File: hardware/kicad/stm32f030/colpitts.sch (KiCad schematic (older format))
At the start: 42 parts, among them P2 LOOP, P3 LOOP, Q1 BSS138, Q2 BC817-40, Q3 BSS138, Q4 BC817-40, T1 78601/9C, T2 78601/9C

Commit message: hardware/kicad/stm32f030: progress
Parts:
- P2: value LOOP -> LOOP1
- P3: value LOOP -> LOOP2
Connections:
- net labels removed: Earth
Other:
- moved on the sheet: GDT2, GDT4, R14, R7

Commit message: hardware/kicad/stm32f030: progress
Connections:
- net at JP1.2, JP1.4, JP1.6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: now also T1.3 (AB); no longer T1.1 (AA)
- net at C5.1, Q1.3 (D), R1.2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: now also T1.1 (AA); no longer T1.3 (AB)
- net at GDT2.1, P2.3 (P3), T1.4 (SA): now also R7.1; no longer GDT1.2
- net at GDT1.1, P2.1 (P1), T1.6 (SB): now also GDT2.2; no longer R7.1
- net at P2.2 (P2), R7.2: now also GDT1.2; no longer GDT2.2
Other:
- moved on the sheet: GDT1, GDT2
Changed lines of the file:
@@
 P 3650 5850
 F 0 "R13" V 3550 5700 50  0000 L CNN
-F 1 "1k" V 3550 5850 50  0000 L CNN
+F 1 "1k" V 3550 5900 50  0000 L CNN
 F 2 "Resistors_SMD:R_0603_HandSoldering" H 3650 5850 50  0001 C CNN
 F 3 "" H 3650 5850 50  0000 C CNN
@@
 F 3 "" H 2600 2550 50  0000 C CNN
 	1    2600 2550
-	-1   0    0    1
+	-1   0    0    -1
 $EndComp
 $Comp
@@
 L GDT GDT1
 U 1 1 5884A6E0
+P 2100 2150
+F 0 "GDT1" H 2110 2040 60  0000 C CNN
+F 1 "GDT" H 2100 2250 60  0000 C CNN
+F 2 "gdt:CG5350L" H 2225 2325 60  0001 C CNN
+F 3 "" H 2225 2325 60  0000 C CNN
+	1    2100 2150
+	0    1    -1   0
+$EndComp
+$Comp
+L GDT GDT2
+U 1 1 5884A6E7
 P 2100 2550
-F 0 "GDT1" H 2110 2440 60  0000 C CNN
+F 0 "GDT2" H 2110 2440 60  0000 C CNN
 F 1 "GDT" H 2100 2650 60  0000 C CNN
 F 2 "gdt:CG5350L" H 2225 2725 60  0001 C CNN
 F 3 "" H 2225 2725 60  0000 C CNN
 	1    2100 2550
-	0    1    -1   0
-$EndComp
-$Comp
-L GDT GDT2
-U 1 1 5884A6E7
-P 2100 2150
-F 0 "GDT2" H 2110 2040 60  0000 C CNN
-F 1 "GDT" H 2100 2250 60  0000 C CNN
-F 2 "gdt:CG5350L" H 2225 2325 60  0001 C CNN
-F 3 "" H 2225 2325 60  0000 C CNN
-	1    2100 2150
 	0    1    -1   0
 $EndComp
@@
 F 3 "" H 1350 2550 50  0000 C CNN
 	1    1350 2550
-	-1   0    0    1
-$EndComp
-$Comp
+	-1   0    0    -1
+$EndComp
+$Comp

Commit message: hardware/kicad/stm32f030: adding eeprom step2
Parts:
- GDT1, GDT2, GDT3, GDT4: footprint gdt:CG5350L -> cardetector:GDT
- T1, T2: footprint murata_pwr:78601_9C -> cardetector:78601_9C
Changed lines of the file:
@@
 F 0 "T2" H 2600 5900 50  0000 C CNN
 F 1 "78601/9C" H 2600 5350 50  0000 C CNN
-F 2 "murata_pwr:78601_9C" H 2600 5650 50  0001 C CNN
+F 2 "cardetector:78601_9C" H 2600 5650 50  0001 C CNN
 F 3 "" H 2600 5650 50  0000 C CNN
 	1    2600 5650
@@
 F 0 "GDT3" H 2110 5540 60  0000 C CNN
 F 1 "GDT" H 2100 5750 60  0000 C CNN
-F 2 "gdt:CG5350L" H 2225 5825 60  0001 C CNN
+F 2 "cardetector:GDT" H 2225 5825 60  0001 C CNN
 F 3 "" H 2225 5825 60  0000 C CNN
 	1    2100 5650
@@
 F 0 "GDT4" H 2110 5140 60  0000 C CNN
 F 1 "GDT" H 2100 5350 60  0000 C CNN
-F 2 "gdt:CG5350L" H 2225 5425 60  0001 C CNN
+F 2 "cardetector:GDT" H 2225 5425 60  0001 C CNN
 F 3 "" H 2225 5425 60  0000 C CNN
 	1    2100 5250
@@
 F 0 "T1" H 2600 2800 50  0000 C CNN
 F 1 "78601/9C" H 2600 2250 50  0000 C CNN
-F 2 "murata_pwr:78601_9C" H 2600 2550 50  0001 C CNN
+F 2 "cardetector:78601_9C" H 2600 2550 50  0001 C CNN
 F 3 "" H 2600 2550 50  0000 C CNN
 	1    2600 2550
@@
 F 0 "GDT1" H 2110 2040 60  0000 C CNN
 F 1 "GDT" H 2100 2250 60  0000 C CNN
-F 2 "gdt:CG5350L" H 2225 2325 60  0001 C CNN
+F 2 "cardetector:GDT" H 2225 2325 60  0001 C CNN
 F 3 "" H 2225 2325 60  0000 C CNN
 	1    2100 2150
@@
 F 0 "GDT2" H 2110 2440 60  0000 C CNN
 F 1 "GDT" H 2100 2650 60  0000 C CNN
-F 2 "gdt:CG5350L" H 2225 2725 60  0001 C CNN
+F 2 "cardetector:GDT" H 2225 2725 60  0001 C CNN
 F 3 "" H 2225 2725 60  0000 C CNN
 	1    2100 2550

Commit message: hardware/kicad/stm32f030: final touches
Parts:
- Q1, Q2, Q3, Q4: footprint TO_SOT_Packages_SMD:SOT-23_Handsoldering -> TO_SOT_Packages_SMD:SOT-23
- R1, R2, R8, R9: footprint Resistors_SMD:R_0603_HandSoldering -> Resistors_SMD:R_0805
- T1, T2: footprint cardetector:78601_9C -> cardetector:Murata_Impulse_Transformer
- ZD1, ZD2, ZD3, ZD4: footprint Diodes_SMD:MELF_Standard -> Diodes_SMD:D_MiniMELF_Standard
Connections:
- net at GDT3.2, GDT4.1, T2.4 (SA): now also P3.1 (P1); no longer P3.3 (P3)
- net at GDT3.1, R14.1, T2.6 (SB): now also P3.3 (P3); no longer P3.1 (P1)
- net at GDT2.1, R7.1, T1.4 (SA): now also P2.1 (P1); no longer P2.3 (P3)
- net at GDT1.1, GDT2.2, T1.6 (SB): now also P2.3 (P3); no longer P2.1 (P1)
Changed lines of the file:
@@
 F 0 "T2" H 2600 5900 50  0000 C CNN
 F 1 "78601/9C" H 2600 5350 50  0000 C CNN
-F 2 "cardetector:78601_9C" H 2600 5650 50  0001 C CNN
+F 2 "cardetector:Murata_Impulse_Transformer" H 2600 5650 50  0001 C CNN
 F 3 "" H 2600 5650 50  0000 C CNN
 	1    2600 5650
@@
 F 3 "" H 1350 5650 50  0000 C CNN
 	1    1350 5650
-	-1   0    0    1
+	-1   0    0    -1
 $EndComp
 $Comp
@@
 F 0 "Q3" H 3850 5950 50  0000 L CNN
 F 1 "BSS138" H 3800 5550 50  0000 L CNN
-F 2 "TO_SOT_Packages_SMD:SOT-23_Handsoldering" H 4200 5725 50  0001 L CIN
+F 2 "TO_SOT_Packages_SMD:SOT-23" H 4200 5725 50  0001 L CIN
 F 3 "" H 4000 5800 50  0000 L CNN
 	1    4000 5800
@@
 F 0 "R9" V 4000 4700 50  0000 L CNN
 F 1 "150" V 4000 4850 50  0000 L CNN
-F 2 "Resistors_SMD:R_0603_HandSoldering" H 4100 4850 50  0001 C CNN
+F 2 "Resistors_SMD:R_0805" H 4100 4850 50  0001 C CNN
 F 3 "" H 4100 4850 50  0000 C CNN
 	1    4100 4850
@@
 F 0 "R8" V 3800 4700 50  0000 L CNN
 F 1 "150" V 3800 4850 50  0000 L CNN
-F 2 "Resistors_SMD:R_0603_HandSoldering" H 3900 4850 50  0001 C CNN
+F 2 "Resistors_SMD:R_0805" H 3900 4850 50  0001 C CNN
 F 3 "" H 3900 4850 50  0000 C CNN
 	1    3900 4850
@@
 F 0 "Q4" H 4750 6200 50  0000 L CNN
 F 1 "BC817-40" H 4550 5800 50  0000 L CNN
-F 2 "TO_SOT_Packages_SMD:SOT-23_Handsoldering" H 5100 5975 50  0001 L CIN
+F 2 "TO_SOT_Packages_SMD:SOT-23" H 5100 5975 50  0001 L CIN
 F 3 "" H 4900 6050 50  0000 L CNN
 	1    4900 6050
@@
 F 0 "ZD3" H 3200 5440 50  0000 C CNN
 F 1 "24V" H 3200 5260 50  0000 C CNN
-F 2 "Diodes_SMD:MELF_Standard" V 3200 5350 50  0001 C CNN
+F 2 "Diodes_SMD:D_MiniMELF_Standard" V 3200 5350 50  0001 C CNN
 F 3 "" V 3200 5350 50  0000 C CNN
 	1    3200 5350
@@
 F 0 "ZD4" H 3200 5740 50  0000 C CNN
 F 1 "24V" H 3200 5560 50  0000 C CNN
-F 2 "Diodes_SMD:MELF_Standard" V 3200 5650 50  0001 C CNN
+F 2 "Diodes_SMD:D_MiniMELF_Standard" V 3200 5650 50  0001 C CNN
 F 3 "" V 3200 5650 50  0000 C CNN
 	1    3200 5650
@@
 F 0 "T1" H 2600 2800 50  0000 C CNN
 F 1 "78601/9C" H 2600 2250 50  0000 C CNN
-F 2 "cardetector:78601_9C" H 2600 2550 50  0001 C CNN
+F 2 "cardetector:Murata_Impulse_Transformer" H 2600 2550 50  0001 C CNN
 F 3 "" H 2600 2550 50  0000 C CNN
 	1    2600 2550
@@
 F 3 "" H 1350 2550 50  0000 C CNN
 	1    1350 2550
-	-1   0    0    -1
+	-1   0    0    1
 $EndComp
 $Comp
@@
 F 0 "Q1" H 3850 2850 50  0000 L CNN
 F 1 "BSS138" H 3800 2450 50  0000 L CNN
-F 2 "TO_SOT_Packages_SMD:SOT-23_Handsoldering" H 4200 2625 50  0001 L CIN
+F 2 "TO_SOT_Packages_SMD:SOT-23" H 4200 2625 50  0001 L CIN
 F 3 "" H 4000 2700 50  0000 L CNN
 	1    4000 2700
@@
 F 0 "R2" V 4000 1600 50  0000 L CNN
 F 1 "150" V 4000 1750 50  0000 L CNN
-F 2 "Resistors_SMD:R_0603_HandSoldering" H 4100 1750 50  0001 C CNN
+F 2 "Resistors_SMD:R_0805" H 4100 1750 50  0001 C CNN
 F 3 "" H 4100 1750 50  0000 C CNN
 	1    4100 1750
@@
 F 0 "R1" V 3800 1600 50  0000 L CNN
 F 1 "150" V 3800 1750 50  0000 L CNN
-F 2 "Resistors_SMD:R_0603_HandSoldering" H 3900 1750 50  0001 C CNN
+F 2 "Resistors_SMD:R_0805" H 3900 1750 50  0001 C CNN
 F 3 "" H 3900 1750 50  0000 C CNN
 	1    3900 1750
@@
 F 0 "Q2" H 4750 3100 50  0000 L CNN
 F 1 "BC817-40" H 4550 2700 50  0000 L CNN
-F 2 "TO_SOT_Packages_SMD:SOT-23_Handsoldering" H 5100 2875 50  0001 L CIN
+F 2 "TO_SOT_Packages_SMD:SOT-23" H 5100 2875 50  0001 L CIN
 F 3 "" H 4900 2950 50  0000 L CNN
 	1    4900 2950
@@
 F 0 "ZD1" H 3200 2340 50  0000 C CNN
 F 1 "24V" H 3200 2160 50  0000 C CNN
-F 2 "Diodes_SMD:MELF_Standard" V 3200 2250 50  0001 C CNN
+F 2 "Diodes_SMD:D_MiniMELF_Standard" V 3200 2250 50  0001 C CNN
 F 3 "" V 3200 2250 50  0000 C CNN
 	1    3200 2250
@@
 F 0 "ZD2" H 3200 2640 50  0000 C CNN
 F 1 "24V" H 3200 2460 50  0000 C CNN
-F 2 "Diodes_SMD:MELF_Standard" V 3200 2550 50  0001 C CNN
+F 2 "Diodes_SMD:D_MiniMELF_Standard" V 3200 2550 50  0001 C CNN
 F 3 "" V 3200 2550 50  0000 C CNN
 	1    3200 2550

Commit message: hardware/kicad/stm32f030: blocks ready
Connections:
- net at JP2.2, JP2.4, JP2.6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: now also T2.3 (AB); no longer T2.1 (AA)
- net at C10.1, Q3.3 (D), R12.1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: now also T2.1 (AA); no longer T2.3 (AB)
- net at P3.1 (P1), T2.4 (SA): now also GDT3.1, R14.1; no longer GDT3.2, GDT4.1
- net at P3.3 (P3), T2.6 (SB): now also GDT3.2, GDT4.1; no longer GDT3.1, R14.1
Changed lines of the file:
@@
 $Descr A4 11693 8268
 encoding utf-8
-Sheet 2 6
+Sheet 2 5
 Title ""
 Date ""
@@
 F 3 "" H 2600 5650 50  0000 C CNN
 	1    2600 5650
-	-1   0    0    1
+	-1   0    0    -1
 $EndComp
 $Comp
@@
 F 3 "" H 1350 5650 50  0000 C CNN
 	1    1350 5650
-	-1   0    0    -1
+	-1   0    0    1
 $EndComp
 $Comp

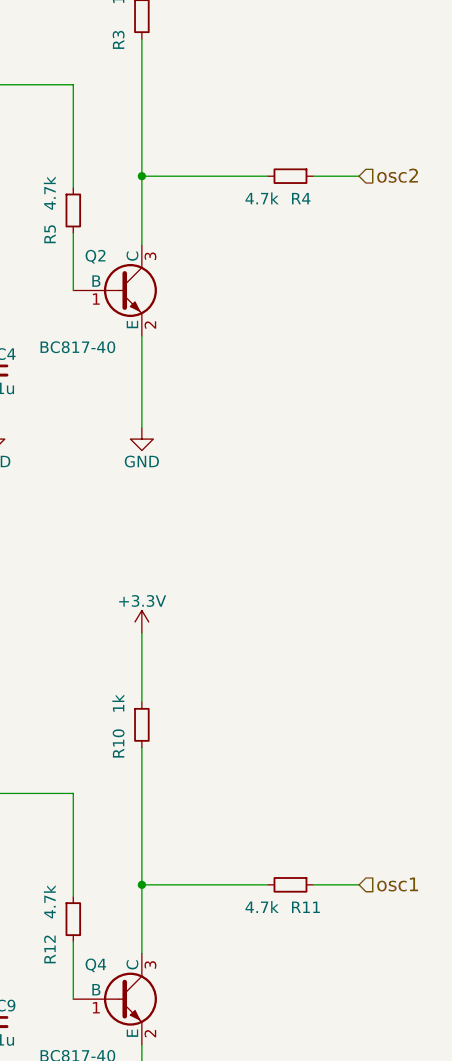
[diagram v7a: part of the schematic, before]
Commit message: hardware/kicad/stm32f030: everything is connected, DRC OK
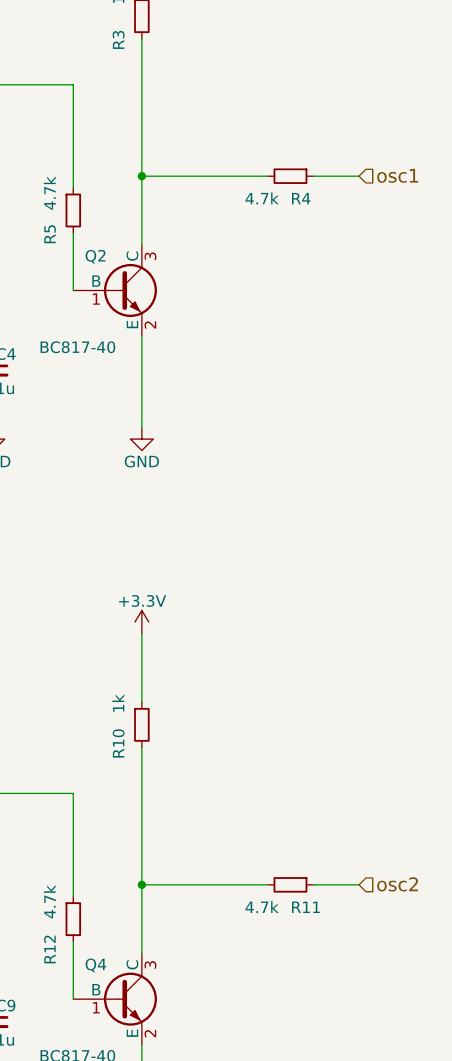
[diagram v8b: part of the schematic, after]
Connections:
- net osc1: now also R4.1; no longer R11.1
- net osc2: now also R11.1; no longer R4.1
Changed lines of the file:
@@
 LIBS:transformer
 LIBS:stm32
+LIBS:switches
 LIBS:stm32f030-cache
 EELAYER 25 0
@@
 	0    1    1    0
 $EndComp
-Text HLabel 5950 5550 2    60   Input ~ 0
+Text HLabel 5950 2450 2    60   Input ~ 0
 osc1
 $Comp
@@
 	0    1    1    0
 $EndComp
-Text HLabel 5950 2450 2    60   Input ~ 0
+Text HLabel 5950 5550 2    60   Input ~ 0
 osc2
 $Comp
